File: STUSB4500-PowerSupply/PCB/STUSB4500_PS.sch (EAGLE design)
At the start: 98 parts, among them J2 FEMALE 2x3, J3 FEMALE 2x3, J4 FEMALE 2x3, SW1 SPST_TACT-EVQQ2

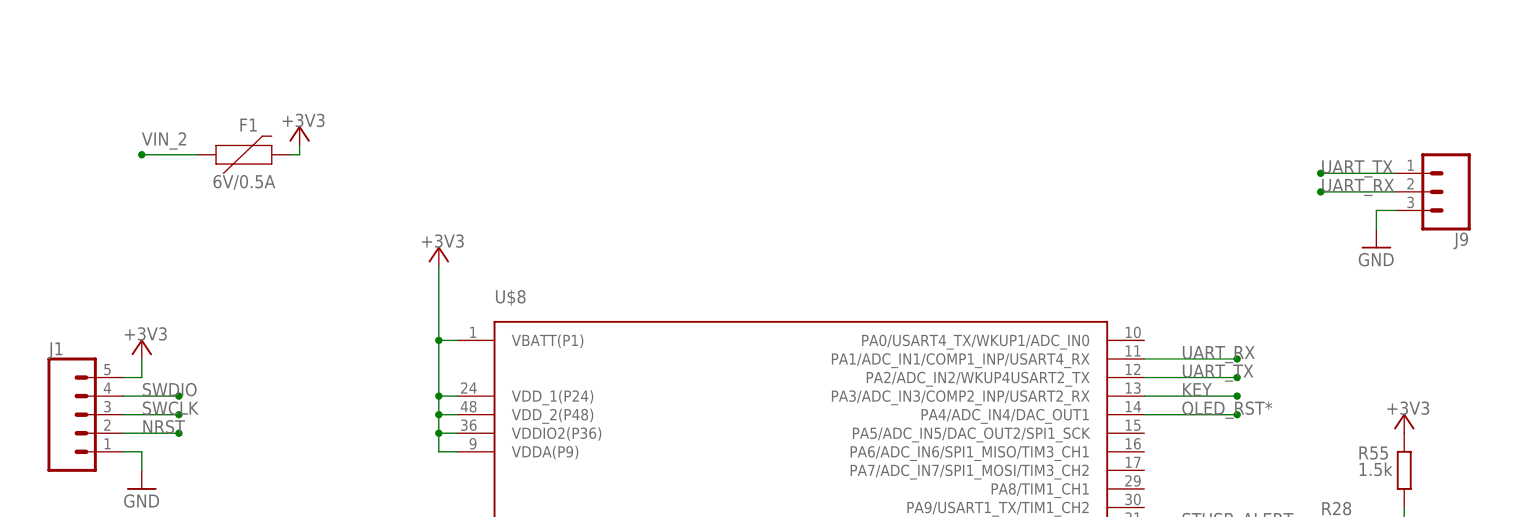
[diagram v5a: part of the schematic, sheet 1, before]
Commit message: Added alternate 3V3 source
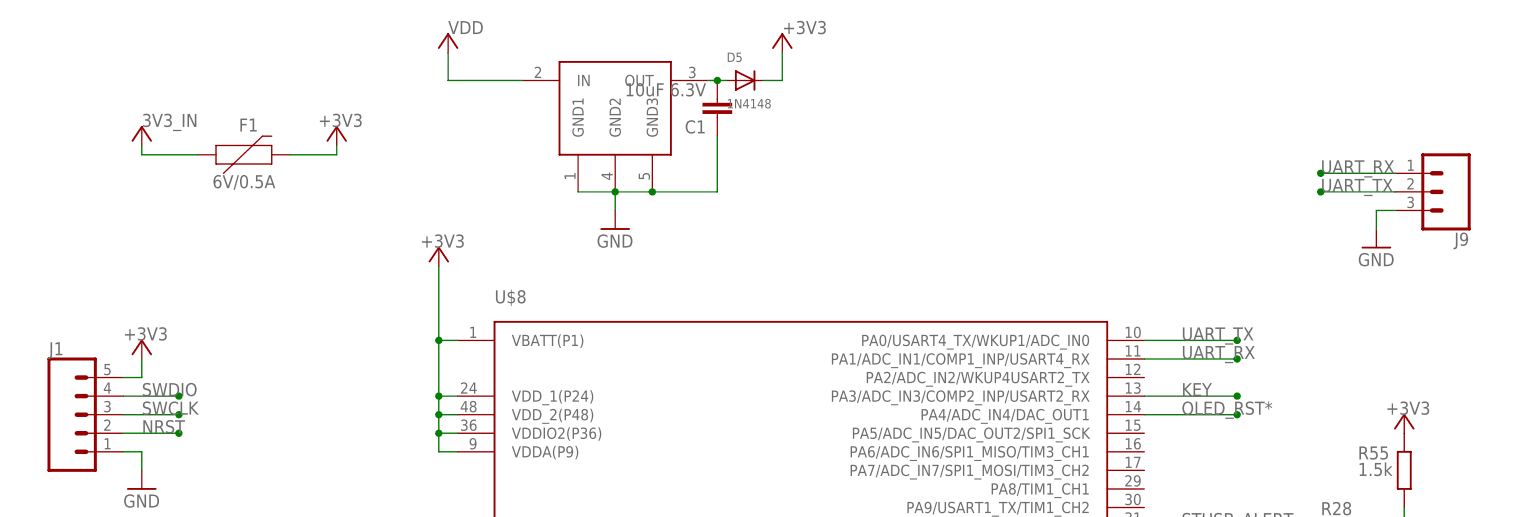
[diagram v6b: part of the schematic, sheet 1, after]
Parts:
- added C1: 10uF 6.3V, DD_rcl:C-EUC0603
- added D5: 1N4148, DD_adafruit:DIODESOD-323F
- added U$1: TLV704_3V3SOT23-5, DD_TLV704:TLV704_3V3SOT23-5
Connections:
- removed net VIN_2: F1.1
- new net N$2: C1.2, D5.A, U$1.OUT
- net +3V3: now also D5.C
- net 3V3_IN: now also F1.1
- net GND: now also C1.1, U$1.GND1, U$1.GND2, U$1.GND3
- net UART_RX: now also J9.1; no longer J9.2
- net UART_TX: now also J9.2, U$8.PA0/USART4_TX/WKUP1/ADC_IN0; no longer J9.1, U$8.PA2/ADC_IN2/WKUP4USART2_TX
- net VDD: now also U$1.IN
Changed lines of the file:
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@@
 <part name="J12" library="DD_SparkFun-Connectors" deviceset="CONN_02" device="1.27"/>
 <part name="J13" library="DD_SparkFun-Connectors" deviceset="CONN_03" device="1.27"/>
+<part name="U$1" library="DD_TLV704" deviceset="TLV704_3V3" device="SOT23-5" package3d_urn="urn:adsk.eagle:package:15955184/2"/>
+<part name="D5" library="DD_adafruit" deviceset="DIODE" device="SOD-323F" package3d_urn="urn:adsk.eagle:package:6240873/1" value="1N4148"/>
+<part name="+3V17" library="supply1" library_urn="urn:adsk.eagle:library:371" deviceset="+3V3" device=""/>
+<part name="GND1" library="supply1" library_urn="urn:adsk.eagle:library:371" deviceset="GND" device=""/>
+<part name="P+1" library="supply1" library_urn="urn:adsk.eagle:library:371" deviceset="VCC" device="" value="VDD"/>
+<part name="P+2" library="supply1" library_urn="urn:adsk.eagle:library:371" deviceset="VCC" device="" value="3V3_IN"/>
+<part name="C1" library="DD_rcl" deviceset="C-EU" device="C0603" package3d_urn="urn:adsk.eagle:package:23616/2" value="10uF 6.3V"/>
 </parts>
 <sheets>
@@
 <attribute name="VALUE" x="54.61" y="149.606" size="1.778" layer="96" font="vector" align="top-center"/>
 </instance>
-<instance part="+3V16" gate="G$1" x="62.23" y="156.21" smashed="yes">
-<attribute name="VALUE" x="59.69" y="156.21" size="1.778" layer="96"/>
+<instance part="+3V16" gate="G$1" x="67.31" y="156.21" smashed="yes">
+<attribute name="VALUE" x="64.77" y="156.21" size="1.778" layer="96"/>
 </instance>
 <instance part="SW1" gate="G$1" x="34.29" y="45.72" smashed="yes" rot="R270">
 <attribute name="NAME" x="31.75" y="39.37" size="1.778" layer="95"/>
+</instance>
+<instance part="U$1" gate="G$1" x="105.41" y="157.48" smashed="yes"/>
+<instance part="D5" gate="G$1" x="123.19" y="162.56" smashed="yes">
+<attribute name="NAME" x="120.65" y="165.1" size="1.27" layer="95"/>
+<attribute name="VALUE" x="120.65" y="158.75" size="1.27" layer="96"/>
+</instance>
+<instance part="+3V17" gate="G$1" x="128.27" y="168.91" smashed="yes">
+<attribute name="VALUE" x="128.27" y="168.91" size="1.778" layer="96"/>
+</instance>
+<instance part="GND1" gate="1" x="105.41" y="142.24" smashed="yes">
+<attribute name="VALUE" x="102.87" y="139.7" size="1.778" layer="96"/>
+</instance>
+<instance part="P+1" gate="VCC" x="82.55" y="168.91" smashed="yes">
+<attribute name="VALUE" x="82.55" y="168.91" size="1.778" layer="96"/>
+</instance>
+<instance part="P+2" gate="VCC" x="40.64" y="156.21" smashed="yes">
+<attribute name="VALUE" x="40.64" y="156.21" size="1.778" layer="96"/>
+</instance>
+<instance part="C1" gate="G$1" x="119.38" y="157.48" smashed="yes" rot="R180">
+<attribute name="NAME" x="117.856" y="157.099" size="1.778" layer="95" rot="R180"/>
+<attribute name="VALUE" x="117.856" y="162.179" size="1.778" layer="96" rot="R180"/>
 </instance>
 </instances>
@@
 <wire x1="209.55" y1="144.78" x2="209.55" y2="142.24" width="0.1524" layer="91"/>
 </segment>
+<segment>
+<pinref part="U$1" gate="G$1" pin="GND1"/>
+<pinref part="U$1" gate="G$1" pin="GND2"/>
+<wire x1="100.33" y1="147.32" x2="105.41" y2="147.32" width="0.1524" layer="91"/>
+<pinref part="U$1" gate="G$1" pin="GND3"/>
+<wire x1="110.49" y1="147.32" x2="105.41" y2="147.32" width="0.1524" layer="91"/>
+<junction x="105.41" y="147.32"/>
+<wire x1="105.41" y1="147.32" x2="105.41" y2="144.78" width="0.1524" layer="91"/>
+<pinref part="GND1" gate="1" pin="GND"/>
+<wire x1="110.49" y1="147.32" x2="119.38" y2="147.32" width="0.1524" layer="91"/>
+<junction x="110.49" y="147.32"/>
+<pinref part="C1" gate="G$1" pin="1"/>
+<wire x1="119.38" y1="147.32" x2="119.38" y2="154.94" width="0.1524" layer="91"/>
+</segment>
 </net>
 <net name="+3V3" class="0">
@@
 <segment>
 <pinref part="F1" gate="G$1" pin="2"/>
-<wire x1="60.96" y1="152.4" x2="62.23" y2="152.4" width="0.1524" layer="91"/>
+<wire x1="60.96" y1="152.4" x2="67.31" y2="152.4" width="0.1524" layer="91"/>
 <pinref part="+3V16" gate="G$1" pin="+3V3"/>
-<wire x1="62.23" y1="152.4" x2="62.23" y2="153.67" width="0.1524" layer="91"/>
+<wire x1="67.31" y1="152.4" x2="67.31" y2="153.67" width="0.1524" layer="91"/>
+</segment>
+<segment>
+<pinref part="D5" gate="G$1" pin="C"/>
+<wire x1="125.73" y1="162.56" x2="128.27" y2="162.56" width="0.1524" layer="91"/>
+<pinref part="+3V17" gate="G$1" pin="+3V3"/>
+<wire x1="128.27" y1="162.56" x2="128.27" y2="166.37" width="0.1524" layer="91"/>
 </segment>
 </net>
@@
 <net name="UART_RX" class="0">
 <segment>
+<pinref part="U$8" gate="G$1" pin="PA1/ADC_IN1/COMP1_INP/USART4_RX"/>
+<wire x1="177.8" y1="124.46" x2="190.5" y2="124.46" width="0.1524" layer="91"/>
+<label x="182.88" y="124.46" size="1.778" layer="95"/>
+<junction x="190.5" y="124.46"/>
+</segment>
+<segment>
+<pinref part="J9" gate="J$1" pin="1"/>
+<wire x1="212.09" y1="149.86" x2="201.93" y2="149.86" width="0.1524" layer="91"/>
+<label x="201.93" y="149.86" size="1.778" layer="95"/>
+<junction x="201.93" y="149.86"/>
+</segment>
+</net>
+<net name="UART_TX" class="0">
+<segment>
+<pinref part="U$8" gate="G$1" pin="PA0/USART4_TX/WKUP1/ADC_IN0"/>
+<wire x1="177.8" y1="127" x2="190.5" y2="127" width="0.1524" layer="91"/>
+<junction x="190.5" y="127"/>
+<label x="182.88" y="127" size="1.778" layer="95"/>
+</segment>
+<segment>
 <pinref part="J9" gate="J$1" pin="2"/>
 <wire x1="212.09" y1="147.32" x2="201.93" y2="147.32" width="0.1524" layer="91"/>
@@
 <junction x="201.93" y="147.32"/>
 </segment>
-<segment>
-<pinref part="U$8" gate="G$1" pin="PA1/ADC_IN1/COMP1_INP/USART4_RX"/>
-<wire x1="177.8" y1="124.46" x2="190.5" y2="124.46" width="0.1524" layer="91"/>
-<label x="182.88" y="124.46" size="1.778" layer="95"/>
-<junction x="190.5" y="124.46"/>
-</segment>
-</net>
-<net name="UART_TX" class="0">
-<segment>
-<pinref part="J9" gate="J$1" pin="1"/>
-<wire x1="212.09" y1="149.86" x2="201.93" y2="149.86" width="0.1524" layer="91"/>
-<label x="201.93" y="149.86" size="1.778" layer="95"/>
-<junction x="201.93" y="149.86"/>
-</segment>
-<segment>
-<pinref part="U$8" gate="G$1" pin="PA2/ADC_IN2/WKUP4USART2_TX"/>
-<wire x1="177.8" y1="121.92" x2="190.5" y2="121.92" width="0.1524" layer="91"/>
-<label x="182.88" y="121.92" size="1.778" layer="95"/>
-<junction x="190.5" y="121.92"/>
-</segment>
-</net>
-<net name="VIN_2" class="0">
+</net>
+<net name="N$2" class="0">
+<segment>
+<pinref part="U$1" gate="G$1" pin="OUT"/>
+<pinref part="D5" gate="G$1" pin="A"/>
+<wire x1="120.65" y1="162.56" x2="119.38" y2="162.56" width="0.1524" layer="91"/>
+<pinref part="C1" gate="G$1" pin="2"/>
+<wire x1="119.38" y1="162.56" x2="118.11" y2="162.56" width="0.1524" layer="91"/>
+<junction x="119.38" y="162.56"/>
+</segment>
+</net>
+<net name="VDD" class="0">
+<segment>
+<pinref part="U$1" gate="G$1" pin="IN"/>
+<wire x1="92.71" y1="162.56" x2="82.55" y2="162.56" width="0.1524" layer="91"/>
+<pinref part="P+1" gate="VCC" pin="VCC"/>
+<wire x1="82.55" y1="166.37" x2="82.55" y2="162.56" width="0.1524" layer="91"/>
+</segment>
+</net>
+<net name="3V3_IN" class="0">
 <segment>
 <pinref part="F1" gate="G$1" pin="1"/>
 <wire x1="48.26" y1="152.4" x2="40.64" y2="152.4" width="0.1524" layer="91"/>
-<label x="40.64" y="153.67" size="1.778" layer="95"/>
-<junction x="40.64" y="152.4"/>
-</segment>
-</net>
+<pinref part="P+2" gate="VCC" pin="VCC"/>
+<wire x1="40.64" y1="152.4" x2="40.64" y2="153.67" width="0.1524" layer="91"/>
+</segment>
+</net>

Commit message: Cleanups
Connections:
- net 3V3_IN renamed DC-DC-3V3
- net 3V3_OUT renamed DC-DC-3V3_OUT
- net 5V0_IN renamed DC-DC-5V0
- net 5V0_OUT renamed DC-DC-5V0_OUT
- net USB-PD_OUT renamed USB-PD_VDD_OUT
- net VDD renamed USB_PD_VDD*
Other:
- moved on the sheet: D5, R13, R17, R18, R28, R29, R33, R34, R37, R38, R39, R40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

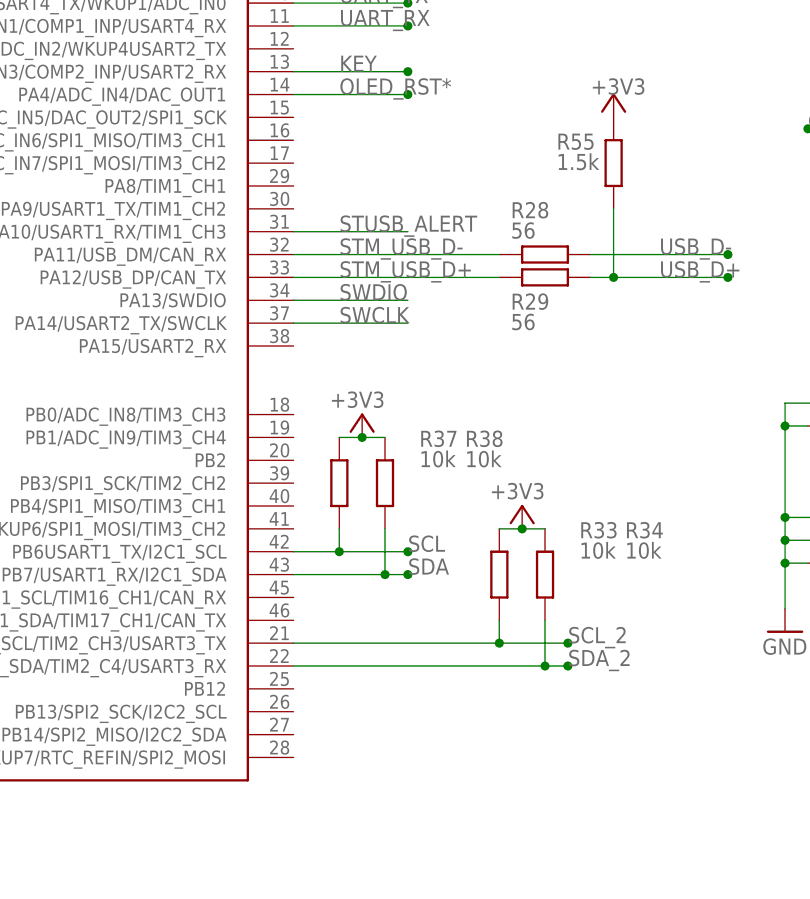
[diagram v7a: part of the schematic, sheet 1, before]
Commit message: Routed additional signals from stusb to stm32 removed teadrops from big pads
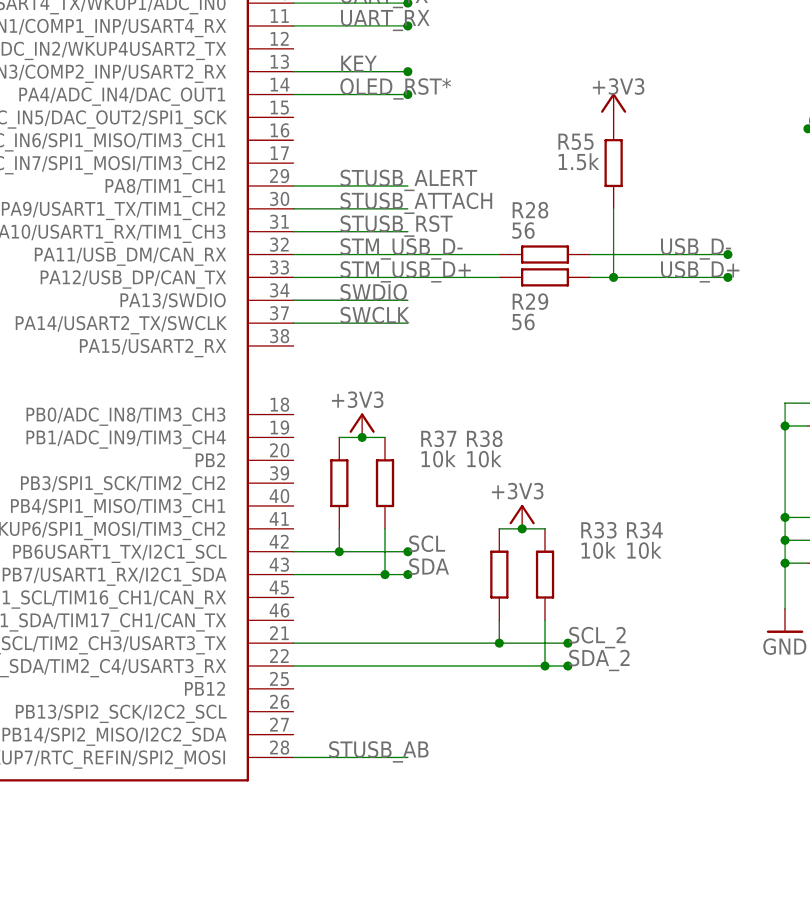
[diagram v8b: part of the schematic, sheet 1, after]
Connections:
- net STUSB_AB: now also U$8.PB15/WKUP7/RTC_REFIN/SPI2_MOSI
- net STUSB_ALERT: now also U$8.PA8/TIM1_CH1; no longer U$8.PA10/USART1_RX/TIM1_CH3
- net STUSB_ATTACH: now also U$8.PA9/USART1_TX/TIM1_CH2
- net STUSB_RST: now also U$8.PA10/USART1_RX/TIM1_CH3
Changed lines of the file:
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@@
-</segment>
-</net>
-<net name="STUSB_ALERT" class="0">
-<segment>
-<pinref part="U$8" gate="G$1" pin="PA10/USART1_RX/TIM1_CH3"/>
-<wire x1="179.07" y1="95.25" x2="191.77" y2="95.25" width="0.1524" layer="91"/>
-<label x="184.15" y="95.25" size="1.778" layer="95"/>
 </segment>
 </net>
@@
 </segment>
 </net>
+<net name="STUSB_ALERT" class="0">
+<segment>
+<pinref part="U$8" gate="G$1" pin="PA8/TIM1_CH1"/>
+<wire x1="179.07" y1="100.33" x2="191.77" y2="100.33" width="0.1524" layer="91"/>
+<label x="184.15" y="100.33" size="1.778" layer="95"/>
+</segment>
+</net>
+<net name="STUSB_RST" class="0">
+<segment>
+<pinref part="U$8" gate="G$1" pin="PA10/USART1_RX/TIM1_CH3"/>
+<wire x1="179.07" y1="95.25" x2="191.77" y2="95.25" width="0.1524" layer="91"/>
+<label x="184.15" y="95.25" size="1.778" layer="95"/>
+</segment>
+</net>
+<net name="STUSB_ATTACH" class="0">
+<segment>
+<pinref part="U$8" gate="G$1" pin="PA9/USART1_TX/TIM1_CH2"/>
+<wire x1="179.07" y1="97.79" x2="191.77" y2="97.79" width="0.1524" layer="91"/>
+<label x="184.15" y="97.79" size="1.778" layer="95"/>
+</segment>
+</net>
+<net name="STUSB_AB" class="0">
+<segment>
+<pinref part="U$8" gate="G$1" pin="PB15/WKUP7/RTC_REFIN/SPI2_MOSI"/>
+<wire x1="179.07" y1="36.83" x2="191.77" y2="36.83" width="0.1524" layer="91"/>
+<label x="182.88" y="36.83" size="1.778" layer="95"/>
+</segment>
+</net>
